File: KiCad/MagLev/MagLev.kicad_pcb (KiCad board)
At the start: 2 copper layers, 120 x 120 mm, 211 parts, among them J1 FC681465S, J2 Programming header, J4 USB_B_Micro, Q1 ZX5T851GTA, Q10 ZX5T851GTA, Q11 MMBT3904, Q12 AOD442G, Q13 AOD442G, Q14 ZX5T851GTA, Q16 TEMT7000X01, Q18 ZX5T1951GTA, Q2 ZX5T1951GTA, Q3 ZX5T851GTA, Q4 ZX5T1951GTA, Q5 ZX5T1951GTA, Q6 ZX5T851GTA, Q7 ZX5T1951GTA, Q8 ZX5T851GTA, Q9 ZX5T1951GTA, U1 LM324, U10 DRV5505, U11 DRV5505, U12 DRV5505, U13 MCP1402, U14 MCP1402, U2 LM324, U3 L78L05_SO8, U4 TL431A, U5 LM393, U6 ATmega328P-A, U8 FT232RL, U9 LM1117MP-5.0, X1 L_Ferrite, X2 L_Ferrite, Y1 L_Ferrite, Y2 L_Ferrite, Y3 J49SMH-16MHz, Y5 L_Ferrite, Y6 L_Ferrite, Y8 L_Ferrite, Y9 L_Ferrite

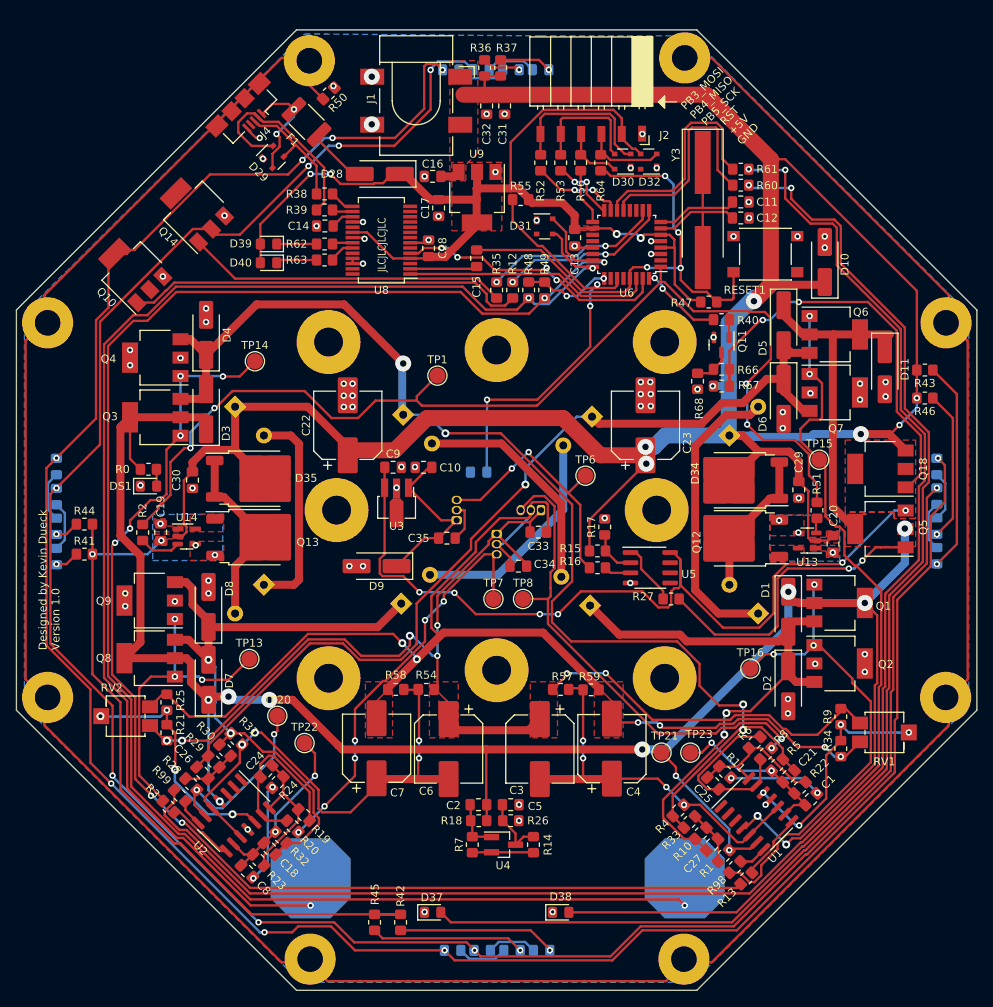
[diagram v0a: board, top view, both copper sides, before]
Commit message: Remove silkscreen components from back layer. Cleanup schematic and pcb.
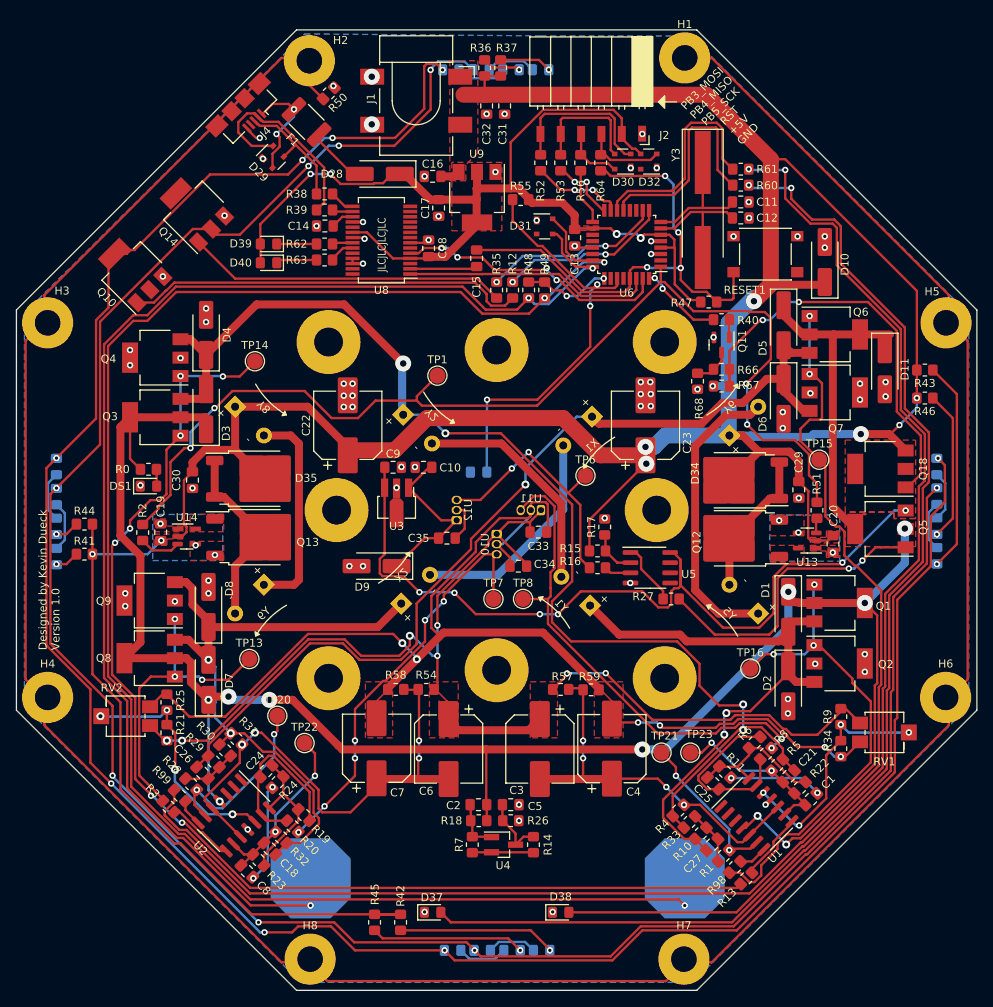
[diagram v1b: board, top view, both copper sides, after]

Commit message: Move op-amps further into board.
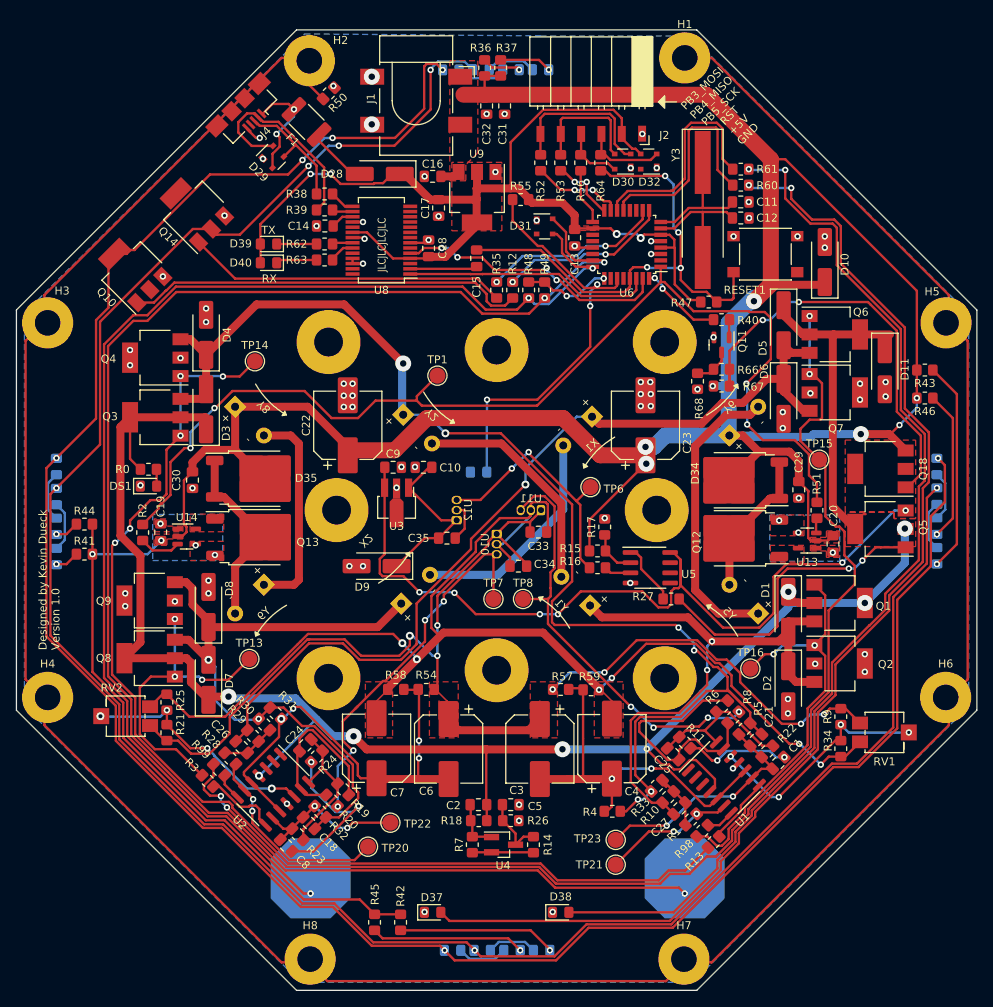
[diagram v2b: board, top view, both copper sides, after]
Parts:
- moved TP20 19.9 mm to (136.3, 143.7)
- moved TP21 15.1 mm to (167.3, 145.9)
- moved TP22 14.6 mm to (139.1, 140.7)
- moved TP23 14.3 mm to (167.3, 142.8)
- moved R4 8.25 mm to (166.8, 139.2), turned to 0 degrees
- moved C25 6.19 mm to (174.4, 132.1)
- moved R11 6.19 mm to (175.9, 130.7)
- moved R10 6.09 mm to (173.8, 137.5)
- moved R22 6.09 mm to (186.2, 131.7)
- moved R8 6.09 mm to (182.0, 127.5)
- moved U1 6.09 mm to (180.8, 135.0)
- moved R6 6.09 mm to (180.6, 126.1)
- moved R13 6.09 mm to (179.5, 143.1)
- moved C1 6.09 mm to (187.6, 133.2)
- moved C21 6.09 mm to (184.8, 130.3)
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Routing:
- net /DR: track 279.4 -> 247.3 mm, vias 10 -> 8
- net Net-(Q6-B): track 167.2 -> 154.9 mm, vias 2 -> 4
- net /Vref-: track 158.3 -> 168.6 mm
- net Net-(U1D--): track 21.7 -> 31.9 mm
- net Net-(C8-Pad1): track 12.6 -> 21.3 mm
- net Net-(U1C--): track 21.1 -> 29.2 mm
- net /H1: track 61.7 -> 53.8 mm, vias 2 -> 4
- net Net-(Q1-B): track 60.1 -> 52.6 mm, vias 3 -> 2
- net Net-(U2B-+): track 60.9 -> 53.4 mm
- net VCC: track 392.3 -> 385.1 mm
- net Net-(D13-K): track 286.9 -> 279.8 mm, vias 8 -> 6
- net Net-(D21-K): track 280.6 -> 274.4 mm, vias 8 -> 6
- net Net-(Q3-B): track 147.5 -> 141.4 mm, vias 7 -> 5
- net /Y2: track 115.2 -> 110.1 mm
- net Net-(D37-A): track 153.1 -> 148.2 mm
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
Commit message: Add underglow.
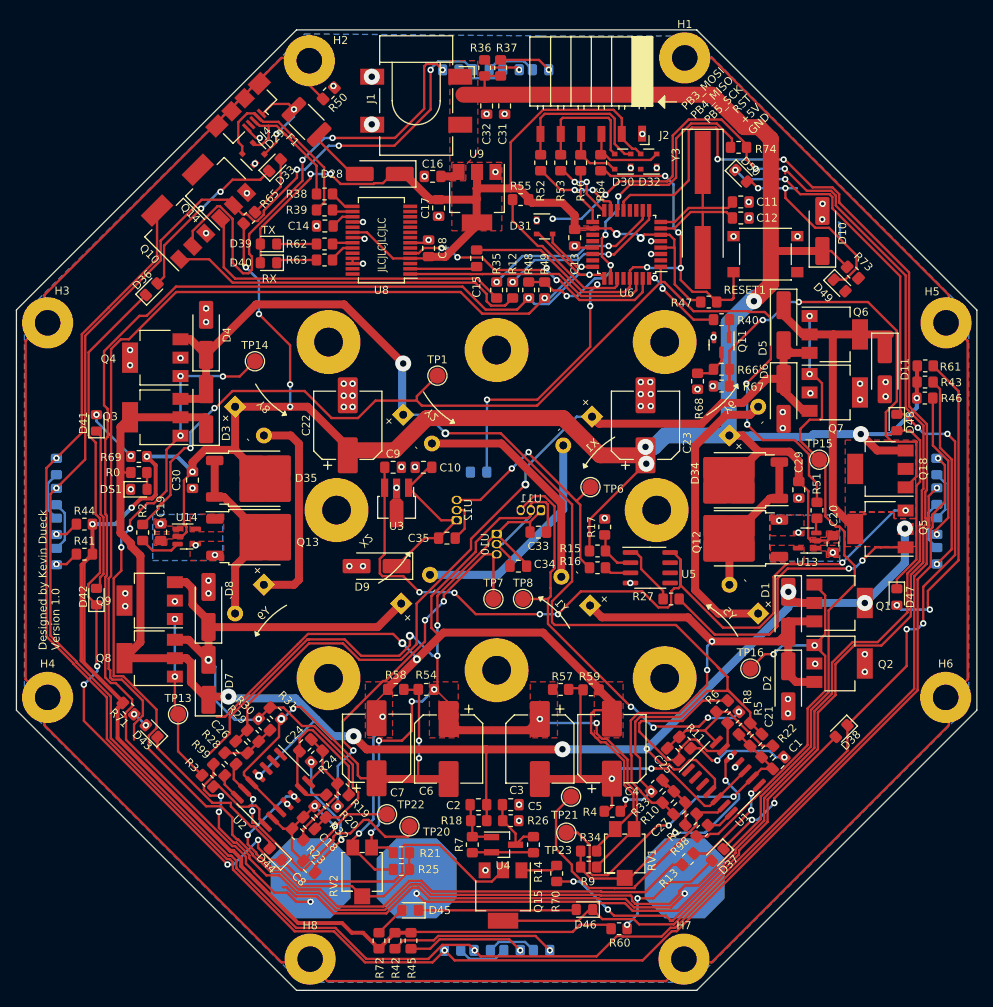
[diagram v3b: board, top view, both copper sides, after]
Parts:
- added D33: LED, LED_SMD:LED_0805_2012Metric_Pad1.15x1.40mm_HandSolder, F.Cu at (124.7, 58.5)
- added D36: LED, LED_SMD:LED_0805_2012Metric_Pad1.15x1.40mm_HandSolder, F.Cu at (109.3, 74.0)
- added D41: LED, LED_SMD:LED_0805_2012Metric_Pad1.15x1.40mm_HandSolder, F.Cu at (102.4, 90.7)
- added D42: LED, LED_SMD:LED_0805_2012Metric_Pad1.15x1.40mm_HandSolder, F.Cu at (102.4, 112.4)
- added D43: LED, LED_SMD:LED_0805_2012Metric_Pad1.15x1.40mm_HandSolder, F.Cu at (109.3, 129.2)
- added D44: LED, LED_SMD:LED_0805_2012Metric_Pad1.15x1.40mm_HandSolder, F.Cu at (124.8, 144.6)
- added D45: LED, LED_SMD:LED_0805_2012Metric_Pad1.15x1.40mm_HandSolder, F.Cu at (141.6, 151.6)
- added D46: LED, LED_SMD:LED_0805_2012Metric_Pad1.15x1.40mm_HandSolder, F.Cu at (163.4, 151.5)
- added D47: LED, LED_SMD:LED_0805_2012Metric_Pad1.15x1.40mm_HandSolder, F.Cu at (202.4, 112.5)
- added D48: LED, LED_SMD:LED_0805_2012Metric_Pad1.15x1.40mm_HandSolder, F.Cu at (202.4, 90.7)
- added D49: LED, LED_SMD:LED_0805_2012Metric_Pad1.15x1.40mm_HandSolder, F.Cu at (195.2, 73.5)
- added D50: LED, LED_SMD:LED_0805_2012Metric_Pad1.15x1.40mm_HandSolder, F.Cu at (182.9, 59.8)
- added PB3: ~, Maglev_Footprint_Library:Capacitive_Touch_Pad, B.Cu at (142.4, 147.6)
- added Q15: ZX5T851GTA, Maglev_Footprint_Library:SOT-223-3_TabPin2_BJT, F.Cu at (153.2, 149.8)
- added R65: 270, Resistor_SMD:R_0805_2012Metric_Pad1.20x1.40mm_HandSolder, F.Cu at (121.5, 65.1)
- added R69: 270, Resistor_SMD:R_0805_2012Metric_Pad1.20x1.40mm_HandSolder, F.Cu at (107.7, 94.9)
- added R70: 1k, Resistor_SMD:R_0805_2012Metric_Pad1.20x1.40mm_HandSolder, F.Cu at (159.9, 147.0)
- added R71: 270, Resistor_SMD:R_0805_2012Metric_Pad1.20x1.40mm_HandSolder, F.Cu at (106.4, 126.4)
- added R72: 270, Resistor_SMD:R_0805_2012Metric_Pad1.20x1.40mm_HandSolder, F.Cu at (137.7, 155.4)
- added R73: 270, Resistor_SMD:R_0805_2012Metric_Pad1.20x1.40mm_HandSolder, F.Cu at (196.9, 71.9)
- added R74: 1M, Resistor_SMD:R_0805_2012Metric_Pad1.20x1.40mm_HandSolder, F.Cu at (182.6, 56.3)
- D37, D38: value Yellow -> LED
- R60, R61: value 145 -> 270
- U12: value DRV5505 -> locked
- moved R60 94.1 mm to (167.7, 153.9)
- moved D38 41.8 mm to (195.5, 129.2), turned to -135 degrees
- moved R9 36.7 mm to (163.9, 146.2), turned to 0 degrees
- moved D37 36.3 mm to (180.0, 144.7), turned to -135 degrees
- moved R25 36.0 mm to (140.5, 146.5), turned to 180 degrees
- moved RV1 35.8 mm to (168.4, 144.5), turned to 90 degrees
- moved RV2 35.4 mm to (135.6, 146.8), turned to 90 degrees
- moved R34 34.0 mm to (163.9, 144.2), turned to 0 degrees
- moved R61 33.7 mm to (205.9, 83.6)
- moved R21 32.9 mm to (140.5, 144.4), turned to 180 degrees
- moved TP13 11.3 mm to (112.6, 127.1)
- moved TP21 10.2 mm to (161.7, 137.4)
- moved Q10 7.62 mm to (112.2, 66.4)
- moved TP23 6.24 mm to (161.1, 141.9)
- moved TP20 5.77 mm to (141.5, 141.1)
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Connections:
- D31 pad 2: unconnected-(D31-K-Pad2) -> /MCU/Touch1
- D31 pad 3: /MCU/Touch1 -> /MCU/Touch2
- D31 pad 4: /MCU/Touch2 -> /MCU/Touch3
- D37 pad 1: GND -> Net-(D37-K)
- D38 pad 1: GND -> Net-(D36-K)
- D38 pad 2: Net-(D38-A) -> Net-(D37-K)
- R60 pad 2: /MCU/LED1 -> VCC
- R61 pad 1: Net-(D38-A) -> Net-(D47-A)
- R61 pad 2: /MCU/LED2 -> VCC
- U6 pad 13: /MCU/LED1 -> /MCU/LED_bot
- U6 pad 14: /MCU/LED2 -> unconnected-(U6-PB2-Pad14)
- U6 pad 23: /MCU/Touch2 -> unconnected-(U6-PC0-Pad23)
- U6 pad 24: /MCU/Touch1 -> /MCU/Touch2
- U6 pad 25: /MCU/TouchCom -> /MCU/Touch1
- U6 pad 26: unconnected-(U6-PC3-Pad26) -> /MCU/TouchCom
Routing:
- net Net-(D36-K): track 0.00 -> 280.0 mm, vias 0 -> 10
- net /MCU/Touch3: track 0.00 -> 191.0 mm, vias 0 -> 5
- net /MCU/LED_bot: track 0.00 -> 168.4 mm, vias 0 -> 4
- net Net-(D37-A): track 148.2 -> 15.1 mm
- net Net-(D38-A): track 132.3 -> 0.00 mm, vias 2 -> 0
- net VCC: track 385.1 -> 452.6 mm, vias 9 -> 14
- net Net-(D47-A): track 0.00 -> 37.8 mm, vias 0 -> 2
- net /MCU/TouchCom: track 11.0 -> 47.3 mm, vias 2 -> 4
- net /MCU/LED1: track 28.2 -> 0.00 mm
- net /MCU/LED2: track 27.9 -> 0.00 mm
- net Net-(D49-K): track 0.00 -> 26.8 mm, vias 0 -> 2
- net /MCU/Touch2: track 205.9 -> 181.5 mm
- net Net-(D47-K): track 0.00 -> 23.3 mm
- net Net-(D33-K): track 0.00 -> 22.1 mm, vias 0 -> 2
- net Net-(D43-K): track 0.00 -> 21.3 mm
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
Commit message: Update LED PCB reference after adding new LED schematic sheet.
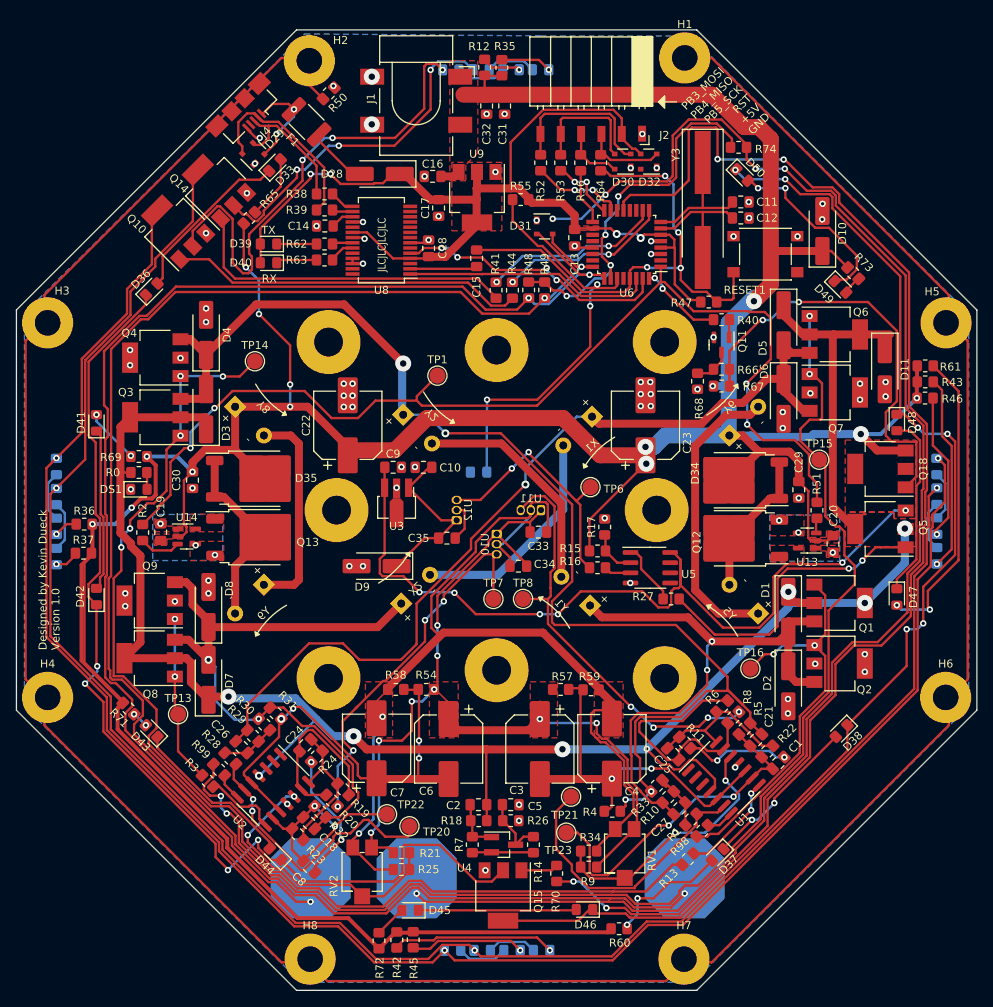
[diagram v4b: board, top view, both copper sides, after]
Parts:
- D12, D13, D14, D15, D16, D17, D18, D19: value LED -> WH
- D20, D21, D22, D23, D24, D25, D26, D27: value LED -> UV
- D33, D36, D37, D38, D41, D42, D43, D44, D45, D46, D47, D48, D49, D50: value LED -> WRM
- R12, R35: value 1k -> 270
- R41, R44: value 270 -> 1k
- moved R37 80.0 mm to (100.8, 107.0), turned to 0 degrees
- moved R36 75.8 mm to (100.9, 103.3), turned to 0 degrees
- moved R41 61.1 mm to (152.3, 74.1), turned to 90 degrees
- moved R44 60.9 mm to (154.4, 74.1), turned to 90 degrees
- moved R12 28.0 mm to (150.9, 46.3), turned to -90 degrees
- moved R35 27.8 mm to (153.1, 46.3), turned to -90 degrees
- moved R45 0.30 mm to (142.0, 155.3)
- moved R42 0.25 mm to (139.9, 155.3)
- moved D49 0.20 mm to (195.4, 73.7)
- moved D50 0.16 mm to (183.1, 59.7)
- moved R73 0.09 mm to (196.9, 72.0)
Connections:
- R12 pad 1: Net-(Q10-B) -> Net-(D12-A)
- R12 pad 2: /MCU/LED_WH -> VCC
- R35 pad 1: Net-(Q14-B) -> Net-(D20-A)
- R35 pad 2: /MCU/LED_UV -> VCC
- R36 pad 1: Net-(D12-A) -> Net-(D14-A)
- R37 pad 1: Net-(D20-A) -> Net-(D22-A)
- R41 pad 1: Net-(D22-A) -> Net-(Q14-B)
- R41 pad 2: VCC -> /MCU/LED_UV
- R44 pad 1: Net-(D14-A) -> Net-(Q10-B)
- R44 pad 2: VCC -> /MCU/LED_WH
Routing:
- net /Vref+: track 156.6 -> 117.3 mm, vias 9 -> 8
- net /Vref-: track 168.0 -> 136.7 mm, vias 4 -> 2
- net /MCU/Touch2: track 181.5 -> 208.0 mm
- net Net-(D49-K): track 26.8 -> 23.4 mm
- net Net-(D49-A): track 0.00 -> 2.29 mm
- net VCC: track 452.6 -> 450.8 mm
- net Net-(D21-K): track 279.7 -> 278.4 mm
- net /MCU/LED_bot: track 168.4 -> 167.5 mm
- net Net-(Q6-B): track 163.4 -> 162.7 mm
- net /X1: track 156.2 -> 155.5 mm
- net Net-(D33-K): track 22.1 -> 21.4 mm, vias 2 -> 0
- net /MCU/Touch3: track 191.0 -> 190.4 mm
- net Net-(D13-K): track 294.2 -> 293.7 mm
- net /MCU/Touch1: track 161.5 -> 160.9 mm
- net Net-(Q10-B): track 44.9 -> 44.4 mm
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
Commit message: Add some PCB art.
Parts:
- added G***: LOGO, Maglev_Footprint_Library:Heart, B.Cu at (159.4, 143.4)
- added G***: LOGO, Maglev_Footprint_Library:Hut, B.Cu at (114.4, 135.0)
- added G***: LOGO, Maglev_Footprint_Library:Eiffel, B.Cu at (184.3, 138.9)
- added G***: LOGO, Maglev_Footprint_Library:Plane, B.Cu at (106.8, 84.9)
- added G***: LOGO, Maglev_Footprint_Library:Splitboard, B.Cu at (113.2, 85.7)
- added G***: LOGO, Maglev_Footprint_Library:BR1, B.Cu at (143.1, 57.1)
- added G***: LOGO, Maglev_Footprint_Library:Stethoscope, B.Cu at (193.0, 125.9)
- added G***: LOGO, Maglev_Footprint_Library:Mountains, B.Cu at (196.6, 101.6)
- added G***: LOGO, Maglev_Footprint_Library:Everest, B.Cu at (191.6, 67.8)
- added G***: LOGO, Maglev_Footprint_Library:Bike, B.Cu at (121.6, 61.6)
- added G***: LOGO, Maglev_Footprint_Library:Golden2, B.Cu at (111.1, 113.9)
- added G***: LOGO, Maglev_Footprint_Library:Wine, B.Cu at (193.1, 83.5)
- added REF**: Top_LED, Maglev_Footprint_Library:Top_LED, B.Cu at (129.2, 140.1)
- added REF**: Power, Maglev_Footprint_Library:Power, B.Cu at (175.9, 138.0)
- added REF**: Bottom_LED, Maglev_Footprint_Library:Bottom_LED, B.Cu at (142.4, 136.1)

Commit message: Add board art folder and upload svg files.
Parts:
- removed the G*** at (114.4, 135.0)
- removed the G*** at (184.3, 138.9)
- removed the G*** at (106.8, 84.9)
- removed the G*** at (113.2, 85.7)
- removed the G*** at (143.1, 57.1)
- removed the G*** at (193.0, 125.9)
- removed the G*** at (196.6, 101.6)
- removed the G*** at (191.6, 67.8)
- removed the G*** at (121.6, 61.6)
- removed the G*** at (111.1, 113.9)
- removed the G*** at (193.1, 83.5)
- added G***: LOGO, Maglev_Footprint_Library:Golden_Silkscreen, B.Cu at (152.1, 57.4)
- C18, C21: value 4.5nF -> 4.7nF
- C24, C25: value 0.4nF -> 470pF
- C26, C27: value 30nF -> 33nF
- D39: value Green -> GREEN
- DS1: value LED -> GREEN
- R0: value 1000 -> 1K
- RV1, RV2: value 10k -> 1k
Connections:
- U1 pad 1: unconnected-(U1-Pad1) -> Net-(U1A--)
- U1 pad 2: unconnected-(U1A---Pad2) -> Net-(U1A--)
- U2 pad 1: unconnected-(U2-Pad1) -> Net-(U2A--)
- U2 pad 2: unconnected-(U2A---Pad2) -> Net-(U2A--)
- U5 pad 6: unconnected-(U5B---Pad6) -> Net-(U5B--)
- U5 pad 7: unconnected-(U5-Pad7) -> Net-(U5B--)
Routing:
- net Net-(U1A--): track 0.00 -> 1.27 mm
- net Net-(U2A--): track 0.00 -> 1.27 mm
- net Net-(U5B--): track 0.00 -> 1.27 mm
